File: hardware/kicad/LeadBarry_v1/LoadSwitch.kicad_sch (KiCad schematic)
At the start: 8 parts, among them Q4 SS9014, Q6 HUF76129S, Q9 BC327

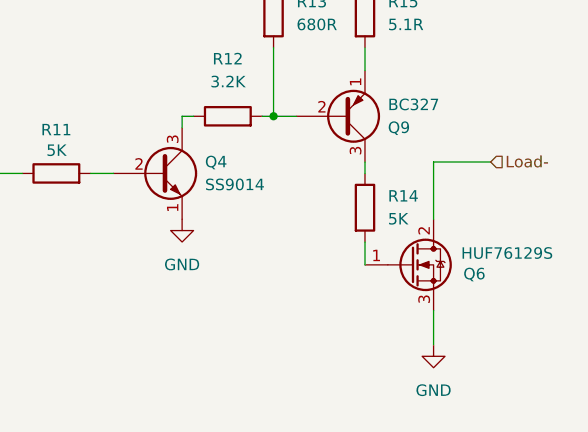
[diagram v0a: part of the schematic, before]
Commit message: fix: implemented regulated voltage schematic
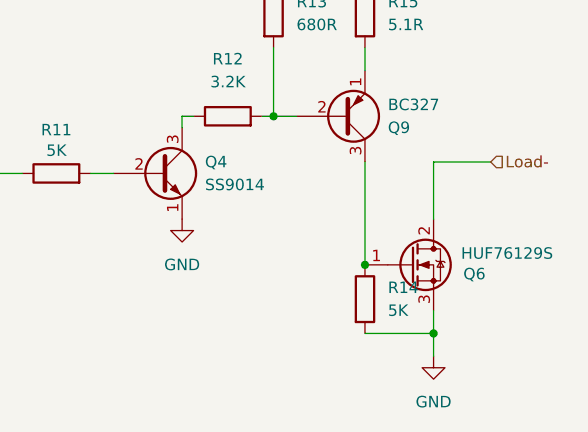
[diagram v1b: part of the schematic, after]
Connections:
- net GND: now also R14.2
- net at Q9.3 (C), R14.1: now also Q6.1 (G)
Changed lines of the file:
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@@
 		(color 0 0 0 0)
 	)
+	(junction
+		(at 119.38 73.66)
+		(diameter 0)
+		(color 0 0 0 0)
+	)
+	(junction
+		(at 127 81.28)
+		(diameter 0)
+		(color 0 0 0 0)
+	)
 	(wire
 		(pts
@@
 	(wire
 		(pts
-			(xy 119.38 73.66) (xy 119.38 71.12)
+			(xy 119.38 62.23) (xy 119.38 73.66)
 		)
 		(stroke
@@
 	(wire
 		(pts
-			(xy 127 82.55) (xy 127 78.74)
+			(xy 127 83.82) (xy 127 81.28)
+		)
+		(stroke
+			(width 0)
+			(type default)
+		)
+	)
+	(wire
+		(pts
+			(xy 119.38 81.28) (xy 127 81.28)
 		)
 		(stroke
@@
 	(wire
 		(pts
-			(xy 119.38 62.23) (xy 119.38 63.5)
+			(xy 127 81.28) (xy 127 78.74)
 		)
 		(stroke
@@
 	(symbol
 		(lib_id "power:GND")
-		(at 127 82.55 0)
+		(at 127 83.82 0)
 		(unit 1)
 		(exclude_from_sim no)
@@
 		(fields_autoplaced yes)
 		(property "Reference" "#PWR013"
+			(at 127 90.17 0)
+			(effects
+				(font
+					(size 1.27 1.27)
+				)
+				(hide yes)
+			)
+		)
+		(property "Value" "GND"
 			(at 127 88.9 0)
 			(effects
@@
 					(size 1.27 1.27)
 				)
-				(hide yes)
-			)
-		)
-		(property "Value" "GND"
-			(at 127 87.63 0)
-			(effects
-				(font
-					(size 1.27 1.27)
-				)
 			)
 		)
 		(property "Footprint" ""
-			(at 127 82.55 0)
+			(at 127 83.82 0)
 			(effects
 				(font
@@
 		)
 		(property "Datasheet" ""
-			(at 127 82.55 0)
+			(at 127 83.82 0)
 			(effects
 				(font
@@
 		)
 		(property "Description" "Power symbol creates a global label with name \"GND\" , ground"
-			(at 127 82.55 0)
+			(at 127 83.82 0)
 			(effects
 				(font
@@
 	(symbol
 		(lib_id "Device:R")
+		(at 119.38 77.47 0)
+		(unit 1)
+		(exclude_from_sim no)
+		(in_bom yes)
+		(on_board yes)
+		(dnp no)
+		(fields_autoplaced yes)
+		(property "Reference" "R14"
+			(at 121.92 76.1999 0)
+			(effects
+				(font
+					(size 1.27 1.27)
+				)
+				(justify left)
+			)
+		)
+		(property "Value" "5K"
+			(at 121.92 78.7399 0)
+			(effects
+				(font
+					(size 1.27 1.27)
+				)
+				(justify left)
+			)
+		)
+		(property "Footprint" "Resistor_THT:R_Axial_DIN0207_L6.3mm_D2.5mm_P10.16mm_Horizontal"
+			(at 117.602 77.47 90)
+			(effects
+				(font
+					(size 1.27 1.27)
+				)
+				(hide yes)
+			)
+		)
+		(property "Datasheet" "~"
+			(at 119.38 77.47 0)
+			(effects
+				(font
+					(size 1.27 1.27)
+				)
+				(hide yes)
+			)
+		)
+		(property "Description" "Resistor"
+			(at 119.38 77.47 0)
+			(effects
+				(font
+					(size 1.27 1.27)
+				)
+				(hide yes)
+			)
+		)
+		(pin "2"
+		)
+		(pin "1"
+		)
+		(instances
+			(project "LeadBarry_v1"
+				(path "/20771d85-0a47-48d4-b39f-5d01020408af/1a5c9110-8742-4ce5-925b-2759184d3a24/eb8485a7-1f6f-4550-85c1-bca6d21a536f"
+					(reference "R14")
+					(unit 1)
+				)
+			)
+		)
+	)
+	(symbol
+		(lib_id "Device:R")
 		(at 119.38 45.72 0)
 		(unit 1)
@@
 					(unit 1)
 				)
-			)
-		)
-	)
-	(symbol
-		(lib_id "Device:R")
-		(at 119.38 67.31 0)
-		(unit 1)
-		(exclude_from_sim no)
-		(in_bom yes)
-		(on_board yes)
-		(dnp no)
-		(fields_autoplaced yes)
-		(property "Reference" "R14"
-			(at 121.92 66.0399 0)
-			(effects
-				(font
-					(size 1.27 1.27)
-				)
-				(justify left)
-			)
-		)
-		(property "Value" "5K"
-			(at 121.92 68.5799 0)
-			(effects
-				(font
-					(size 1.27 1.27)
-				)
-				(justify left)
-			)
-		)
-		(property "Footprint" "Resistor_THT:R_Axial_DIN0207_L6.3mm_D2.5mm_P10.16mm_Horizontal"
-			(at 117.602 67.31 90)
-			(effects
-				(font
-					(size 1.27 1.27)
-				)
-				(hide yes)
-			)
-		)
-		(property "Datasheet" "~"
-			(at 119.38 67.31 0)
-			(effects
-				(font
-					(size 1.27 1.27)
-				)
-				(hide yes)
-			)
-		)
-		(property "Description" "Resistor"
-			(at 119.38 67.31 0)
-			(effects
-				(font
-					(size 1.27 1.27)
-				)
-				(hide yes)
-			)
-		)
-		(pin "2"
-		)
-		(pin "1"
-		)
-		(instances
-			(project "LeadBarry_v1"
-				(path "/20771d85-0a47-48d4-b39f-5d01020408af/1a5c9110-8742-4ce5-925b-2759184d3a24/eb8485a7-1f6f-4550-85c1-bca6d21a536f"
-					(reference "R14")
-					(unit 1)
-				)

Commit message: fix: PoE sockets and DC output status leds were added
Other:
- title: (none) -> Load Switch
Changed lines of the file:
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@@
 	(generator_version "8.0")
 	(paper "A4")
+	(title_block
+		(title "Load Switch")
+		(date "2026-03-21")
+	)
 	(junction
 		(at 109.22 57.15)

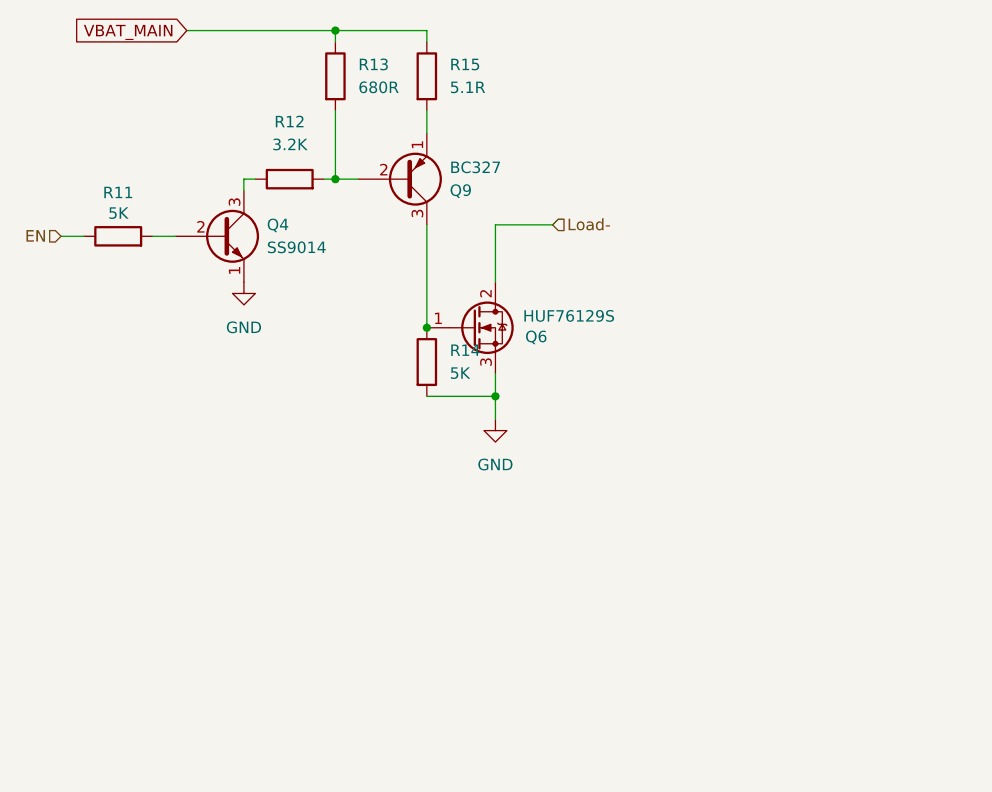
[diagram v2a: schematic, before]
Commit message: fix: added display and timer to the schematic
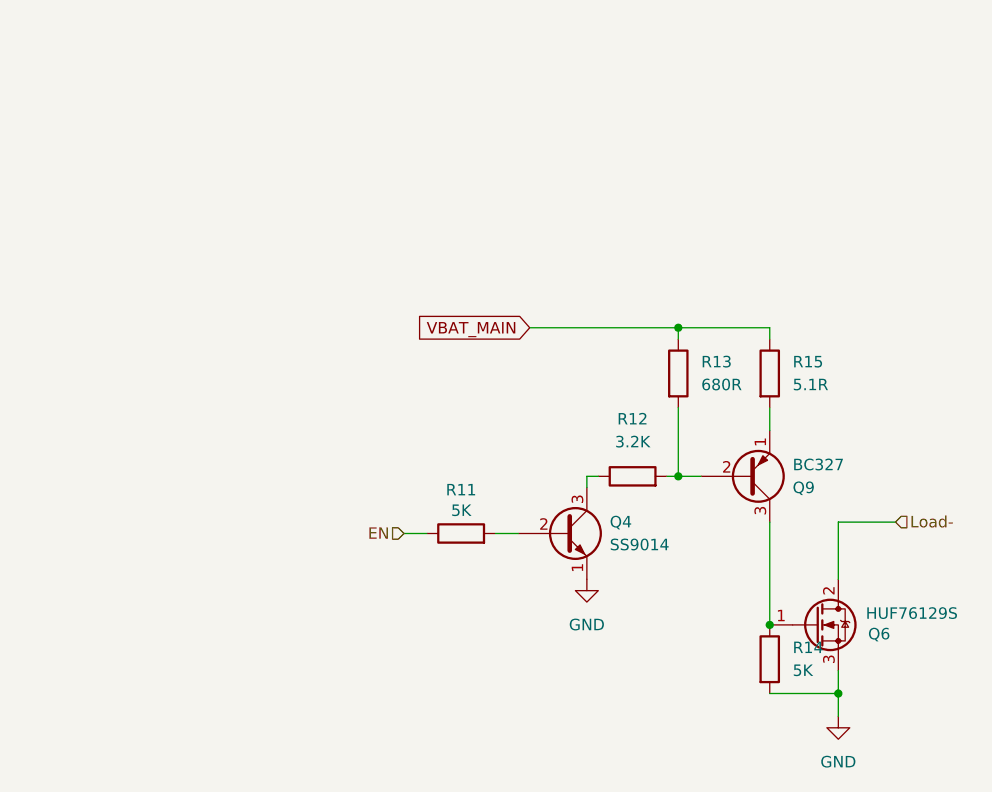
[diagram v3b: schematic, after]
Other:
- moved on the sheet: Q4, Q6, Q9, R11, R12, R13, R14, R15

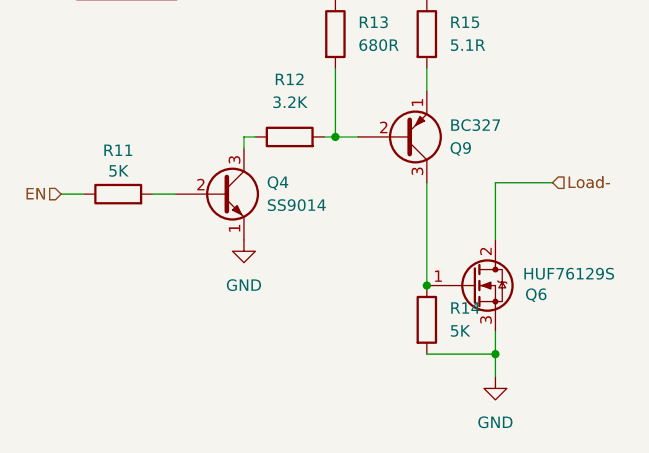
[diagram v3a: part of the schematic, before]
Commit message: fix: RS485 port schematic implemented. Added shift+latch register as a port extension to control the DC outputs.
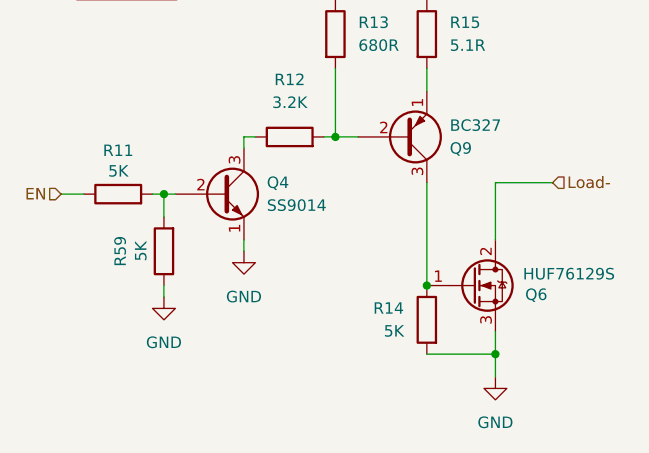
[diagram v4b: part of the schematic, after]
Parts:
- added R59: 5K, Resistor_THT:R_Axial_DIN0207_L6.3mm_D2.5mm_P10.16mm_Horizontal, symbol Device:R
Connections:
- net GND: now also R59.1
- net at Q4.2 (B), R11.2: now also R59.2
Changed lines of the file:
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@@
 		(color 0 0 0 0)
 	)
+	(junction
+		(at 128.27 96.52)
+		(diameter 0)
+		(color 0 0 0 0)
+	)
 	(wire
 		(pts
@@
 	(wire
 		(pts
+			(xy 128.27 96.52) (xy 128.27 99.06)
+		)
+		(stroke
+			(width 0)
+			(type default)
+		)
+	)
+	(wire
+		(pts
 			(xy 147.32 82.55) (xy 147.32 90.17)
 		)
@@
 	(wire
 		(pts
+			(xy 128.27 96.52) (xy 129.54 96.52)
+		)
+		(stroke
+			(width 0)
+			(type default)
+		)
+	)
+	(wire
+		(pts
+			(xy 137.16 101.6) (xy 137.16 102.87)
+		)
+		(stroke
+			(width 0)
+			(type default)
+		)
+	)
+	(wire
+		(pts
 			(xy 165.1 95.25) (xy 165.1 101.6)
 		)
@@
 	(wire
 		(pts
+			(xy 128.27 106.68) (xy 128.27 107.95)
+		)
+		(stroke
+			(width 0)
+			(type default)
+		)
+	)
+	(wire
+		(pts
 			(xy 138.43 90.17) (xy 137.16 90.17)
 		)
@@
 	(wire
 		(pts
-			(xy 165.1 116.84) (xy 165.1 114.3)
+			(xy 147.32 73.66) (xy 147.32 74.93)
+		)
+		(stroke
+			(width 0)
+			(type default)
+		)
+	)
+	(wire
+		(pts
+			(xy 147.32 73.66) (xy 157.48 73.66)
+		)
+		(stroke
+			(width 0)
+			(type default)
+		)
+	)
+	(wire
+		(pts
+			(xy 165.1 95.25) (xy 171.45 95.25)
 		)
 		(stroke
@@
 	(wire
 		(pts
-			(xy 147.32 73.66) (xy 147.32 74.93)
-		)
-		(stroke
-			(width 0)
-			(type default)
-		)
-	)
-	(wire
-		(pts
-			(xy 147.32 73.66) (xy 157.48 73.66)
-		)
-		(stroke
-			(width 0)
-			(type default)
-		)
-	)
-	(wire
-		(pts
-			(xy 165.1 95.25) (xy 171.45 95.25)
-		)
-		(stroke
-			(width 0)
-			(type default)
-		)
-	)
-	(wire
-		(pts
-			(xy 165.1 114.3) (xy 165.1 111.76)
+			(xy 165.1 111.76) (xy 165.1 114.3)
 		)
 		(stroke
@@
 	(wire
 		(pts
+			(xy 165.1 114.3) (xy 165.1 116.84)
+		)
+		(stroke
+			(width 0)
+			(type default)
+		)
+	)
+	(wire
+		(pts
 			(xy 147.32 90.17) (xy 149.86 90.17)
 		)
@@
 	(wire
 		(pts
-			(xy 127 96.52) (xy 129.54 96.52)
+			(xy 127 96.52) (xy 128.27 96.52)
 		)
 		(stroke
@@
 	)
 	(symbol
+		(lib_id "Device:R")
+		(at 128.27 102.87 180)
+		(unit 1)
+		(exclude_from_sim no)
+		(in_bom yes)
+		(on_board yes)
+		(dnp no)
+		(property "Reference" "R59"
+			(at 123.444 102.87 90)
+			(effects
+				(font
+					(size 1.27 1.27)
+				)
+			)
+		)
+		(property "Value" "5K"
+			(at 125.73 102.87 90)
+			(effects
+				(font
+					(size 1.27 1.27)
+				)
+			)
+		)
+		(property "Footprint" "Resistor_THT:R_Axial_DIN0207_L6.3mm_D2.5mm_P10.16mm_Horizontal"
+			(at 130.048 102.87 90)
+			(effects
+				(font
+					(size 1.27 1.27)
+				)
+				(hide yes)
+			)
+		)
+		(property "Datasheet" "~"
+			(at 128.27 102.87 0)
+			(effects
+				(font
+					(size 1.27 1.27)
+				)
+				(hide yes)
+			)
+		)
+		(property "Description" "Resistor"
+			(at 128.27 102.87 0)
+			(effects
+				(font
+					(size 1.27 1.27)
+				)
+				(hide yes)
+			)
+		)
+		(pin "2"
+		)
+		(pin "1"
+		)
+		(instances
+			(project "LeadBarry_v1"
+				(path "/20771d85-0a47-48d4-b39f-5d01020408af/1a5c9110-8742-4ce5-925b-2759184d3a24/eb8485a7-1f6f-4550-85c1-bca6d21a536f"
+					(reference "R59")
+					(unit 1)
+				)
+			)
+		)
+	)
+	(symbol
 		(lib_id "Transistor_FET:IRFZ44NSTRLPBF")
 		(at 162.56 106.68 0)
@@
 		(lib_id "Device:R")
 		(at 157.48 110.49 0)
-		(unit 1)
-		(exclude_from_sim no)
-		(in_bom yes)
-		(on_board yes)
-		(dnp no)
-		(fields_autoplaced yes)
+		(mirror y)
+		(unit 1)
+		(exclude_from_sim no)
+		(in_bom yes)
+		(on_board yes)
+		(dnp no)
 		(property "Reference" "R14"
-			(at 160.02 109.2199 0)
+			(at 154.94 109.2199 0)
 			(effects
 				(font
@@
 		)
 		(property "Value" "5K"
-			(at 160.02 111.7599 0)
+			(at 154.94 111.7599 0)
 			(effects
 				(font
@@
 		)
 		(property "Footprint" "Resistor_THT:R_Axial_DIN0207_L6.3mm_D2.5mm_P10.16mm_Horizontal"
-			(at 155.702 110.49 90)
+			(at 159.258 110.49 90)
 			(effects
 				(font
@@
 	(symbol
 		(lib_id "power:GND")
-		(at 137.16 101.6 0)
+		(at 137.16 102.87 0)
 		(unit 1)
 		(exclude_from_sim no)
@@
 		(fields_autoplaced yes)
 		(property "Reference" "#PWR014"
+			(at 137.16 109.22 0)
+			(effects
+				(font
+					(size 1.27 1.27)
+				)
+				(hide yes)
+			)
+		)
+		(property "Value" "GND"
 			(at 137.16 107.95 0)
 			(effects
@@
 					(size 1.27 1.27)
 				)
-				(hide yes)
-			)
-		)
-		(property "Value" "GND"
-			(at 137.16 106.68 0)
-			(effects
-				(font
-					(size 1.27 1.27)
-				)
 			)
 		)
 		(property "Footprint" ""
-			(at 137.16 101.6 0)
+			(at 137.16 102.87 0)
 			(effects
 				(font
@@
 		)
 		(property "Datasheet" ""
-			(at 137.16 101.6 0)
+			(at 137.16 102.87 0)
 			(effects
 				(font
@@
 		)
 		(property "Description" "Power symbol creates a global label with name \"GND\" , ground"
-			(at 137.16 101.6 0)
+			(at 137.16 102.87 0)
 			(effects
 				(font
@@
 					(unit 1)
 				)
+			)
+		)
+	)
+	(symbol
+		(lib_id "power:GND")
+		(at 128.27 107.95 0)
+		(unit 1)
+		(exclude_from_sim no)
+		(in_bom yes)
+		(on_board yes)
+		(dnp no)
+		(fields_autoplaced yes)
+		(property "Reference" "#PWR093"
+			(at 128.27 114.3 0)
+			(effects
+				(font
+					(size 1.27 1.27)
+				)
+				(hide yes)
+			)
+		)
+		(property "Value" "GND"
+			(at 128.27 113.03 0)
+			(effects
+				(font
+					(size 1.27 1.27)
+				)
+			)
+		)
+		(property "Footprint" ""
+			(at 128.27 107.95 0)
+			(effects
+				(font
+					(size 1.27 1.27)
+				)
+				(hide yes)
+			)
+		)
+		(property "Datasheet" ""
+			(at 128.27 107.95 0)
+			(effects
+				(font
+					(size 1.27 1.27)
+				)
+				(hide yes)
+			)
+		)
+		(property "Description" "Power symbol creates a global label with name \"GND\" , ground"
+			(at 128.27 107.95 0)
+			(effects
+				(font
+					(size 1.27 1.27)
+				)
+				(hide yes)
+			)
+		)
+		(pin "1"
+		)
+		(instances
+			(project "LeadBarry_v1"
+				(path "/20771d85-0a47-48d4-b39f-5d01020408af/1a5c9110-8742-4ce5-925b-2759184d3a24/eb8485a7-1f6f-4550-85c1-bca6d21a536f"
+					(reference "#PWR093")
+					(unit 1)
+				)
